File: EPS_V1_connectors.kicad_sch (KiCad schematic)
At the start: 29 parts, among them J1 Conn_01x20_Socket, J2 Conn_01x30_Socket, J3 Conn_01x15_Socket, J4 Conn_01x04_Socket, SW1 SWITCH, SW2 SWITCH, SW3 SWITCH, U4 MP28167GQ-Z

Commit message: Clean up & add labels
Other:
- note added: "CHARGING INPUT"
- note added: "CHARGING OUTPUT"
- note added: "CONNECTORS"
- note added: "GROUND LEG INHIBIT"
- note added: "SOLAR VOLTAGE REGULATOR"
- moved on the sheet: D1, D2, D3, D4, D5, D6, J1, J2, J3, J4, SW1, SW2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

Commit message: Add notes from Harvey meeting
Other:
- note added: "MOS enable"
- note added: "MOSFET bridge, look for low RDS on MOSFET: BUK7M15-60EX Chip: https://www.analog.com/en/products/lt4322.html"

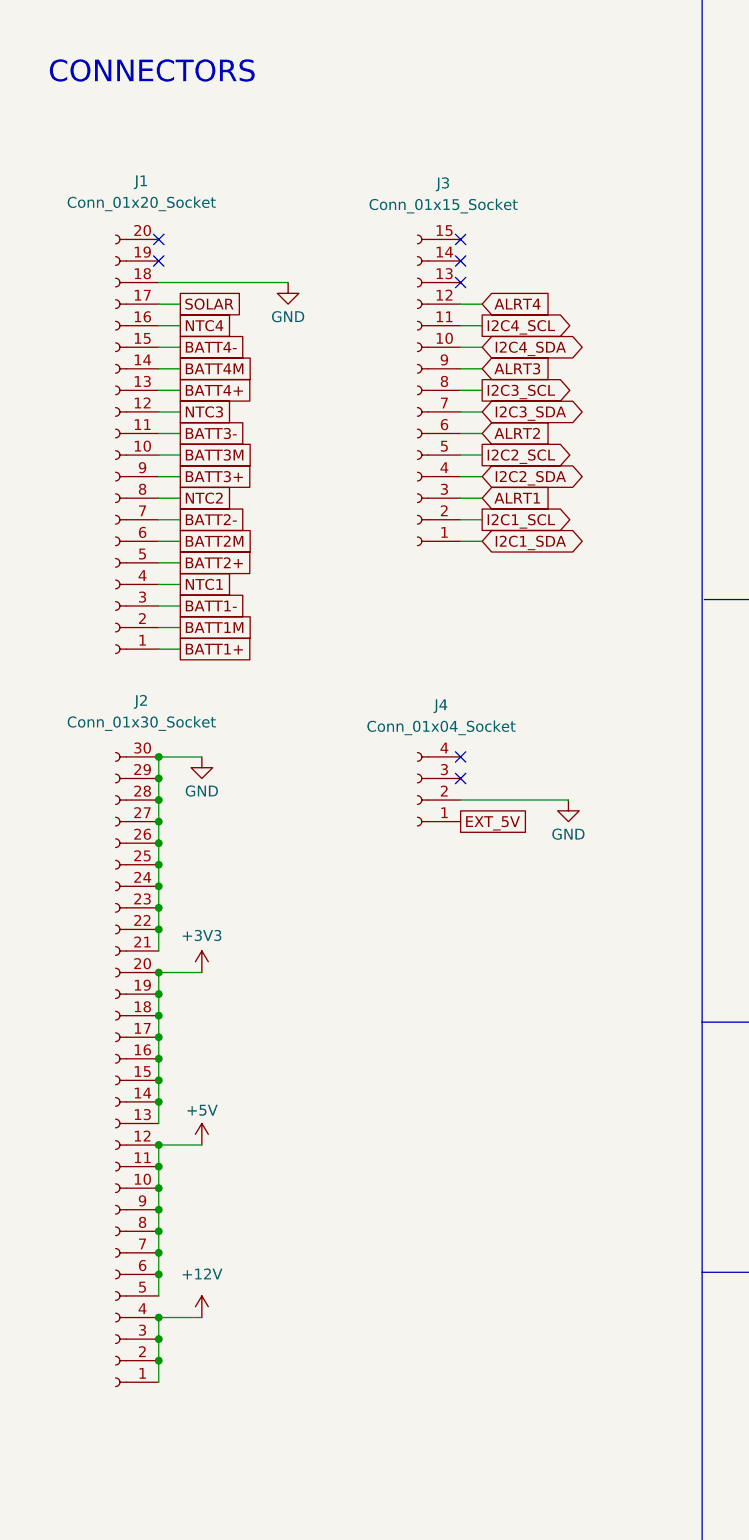
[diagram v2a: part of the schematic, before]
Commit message: assigned footprints to headers
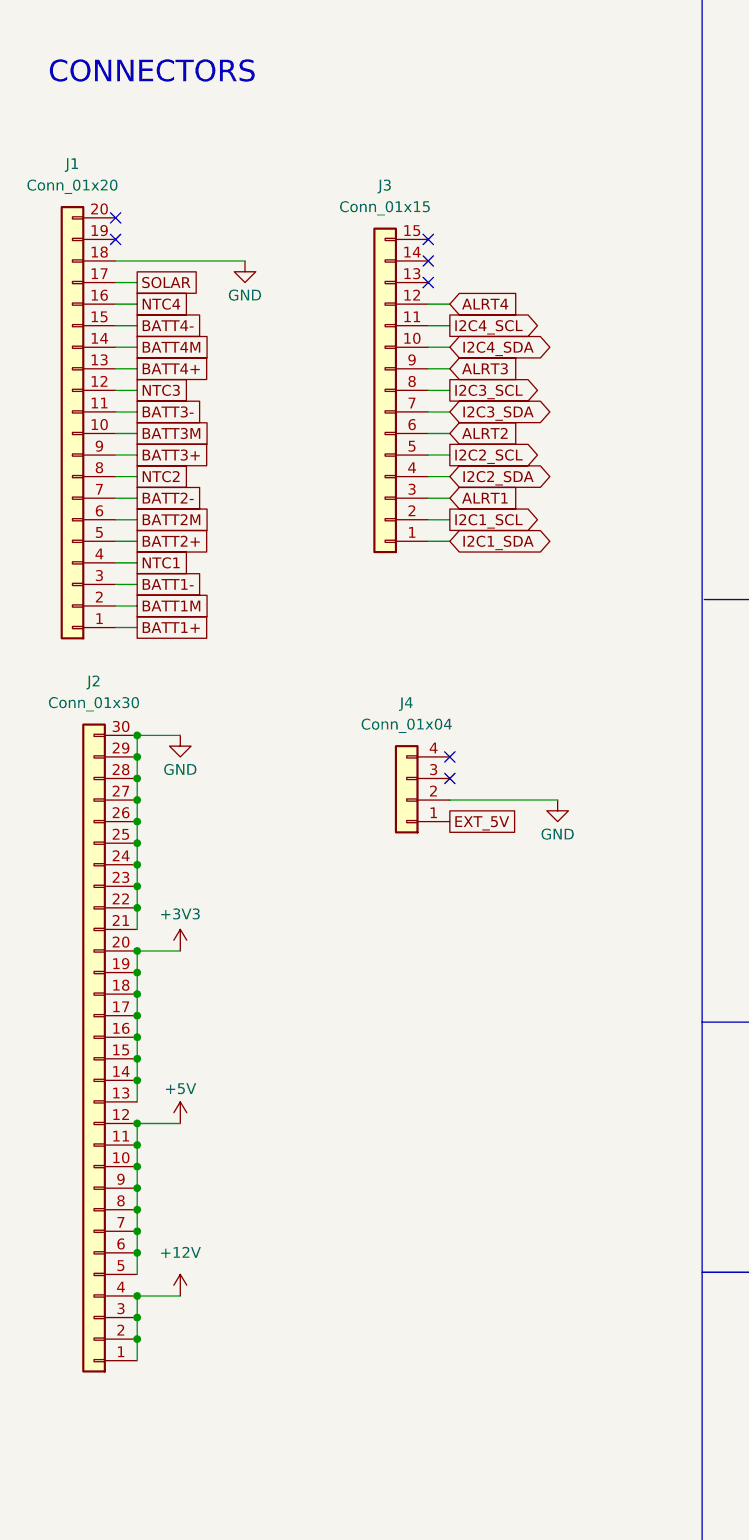
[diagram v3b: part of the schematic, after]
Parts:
- removed J1: Conn_01x20_Socket, symbol Connector:Conn_01x20_Socket
- removed J2: Conn_01x30_Socket, symbol Connector:Conn_01x30_Socket
- removed J3: Conn_01x15_Socket, symbol Connector:Conn_01x15_Socket
- removed J4: Conn_01x04_Socket, symbol Connector:Conn_01x04_Socket
- added J1: Conn_01x20, Connector_IDC:IDC-Header_2x10_P2.54mm_Latch6.5mm_Vertical, symbol Connector_Generic:Conn_01x20
- added J2: Conn_01x30, Connector_PinHeader_2.54mm:PinHeader_1x30_P2.54mm_Vertical, symbol Connector_Generic:Conn_01x30
- added J3: Conn_01x15, symbol Connector_Generic:Conn_01x15
- added J4: Conn_01x04, Connector_PinHeader_2.54mm:PinHeader_1x04_P2.54mm_Vertical, symbol Connector_Generic:Conn_01x04
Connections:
- net ALRT1: now also J3.3 (Pin_3)
- net ALRT2: now also J3.6 (Pin_6)
- net ALRT3: now also J3.9 (Pin_9)
- net ALRT4: now also J3.12 (Pin_12)
- net BATT1+: now also J1.1 (Pin_1)
- net BATT1-: now also J1.3 (Pin_3)
- net BATT1M: now also J1.2 (Pin_2)
- net BATT2+: now also J1.5 (Pin_5)
- net BATT2-: now also J1.7 (Pin_7)
- net BATT2M: now also J1.6 (Pin_6)
- net BATT3+: now also J1.9 (Pin_9)
- net BATT3-: now also J1.11 (Pin_11)
- net BATT3M: now also J1.10 (Pin_10)
- net BATT4+: now also J1.13 (Pin_13)
- net BATT4-: now also J1.15 (Pin_15)
- net BATT4M: now also J1.14 (Pin_14)
- net EXT_5V: now also J4.1 (Pin_1)
- net GND: now also J1.18 (Pin_18), J2.21 (Pin_21), J2.22 (Pin_22), J2.23 (Pin_23), J2.24 (Pin_24), J2.25 (Pin_25), J2.26 (Pin_26), J2.27 (Pin_27), J2.28 (Pin_28), J2.29 (Pin_29), J2.30 (Pin_30), J4.2 (Pin_2)
- net I2C1_SCL: now also J3.2 (Pin_2)
- net I2C1_SDA: now also J3.1 (Pin_1)
- net I2C2_SCL: now also J3.5 (Pin_5)
- net I2C2_SDA: now also J3.4 (Pin_4)
- net I2C3_SCL: now also J3.8 (Pin_8)
- net I2C3_SDA: now also J3.7 (Pin_7)
- net I2C4_SCL: now also J3.11 (Pin_11)
- net I2C4_SDA: now also J3.10 (Pin_10)
- net NTC1: now also J1.4 (Pin_4)
- net NTC2: now also J1.8 (Pin_8)
- net NTC3: now also J1.12 (Pin_12)
- net NTC4: now also J1.16 (Pin_16)
- net SOLAR: now also J1.17 (Pin_17)
- new net: J2.1 (Pin_1), J2.2 (Pin_2), J2.3 (Pin_3), J2.4 (Pin_4)
- new net: J2.10 (Pin_10), J2.11 (Pin_11), J2.12 (Pin_12), J2.5 (Pin_5), J2.6 (Pin_6), J2.7 (Pin_7), J2.8 (Pin_8), J2.9 (Pin_9)
- new net: J2.13 (Pin_13), J2.14 (Pin_14), J2.15 (Pin_15), J2.16 (Pin_16), J2.17 (Pin_17), J2.18 (Pin_18), J2.19 (Pin_19), J2.20 (Pin_20)

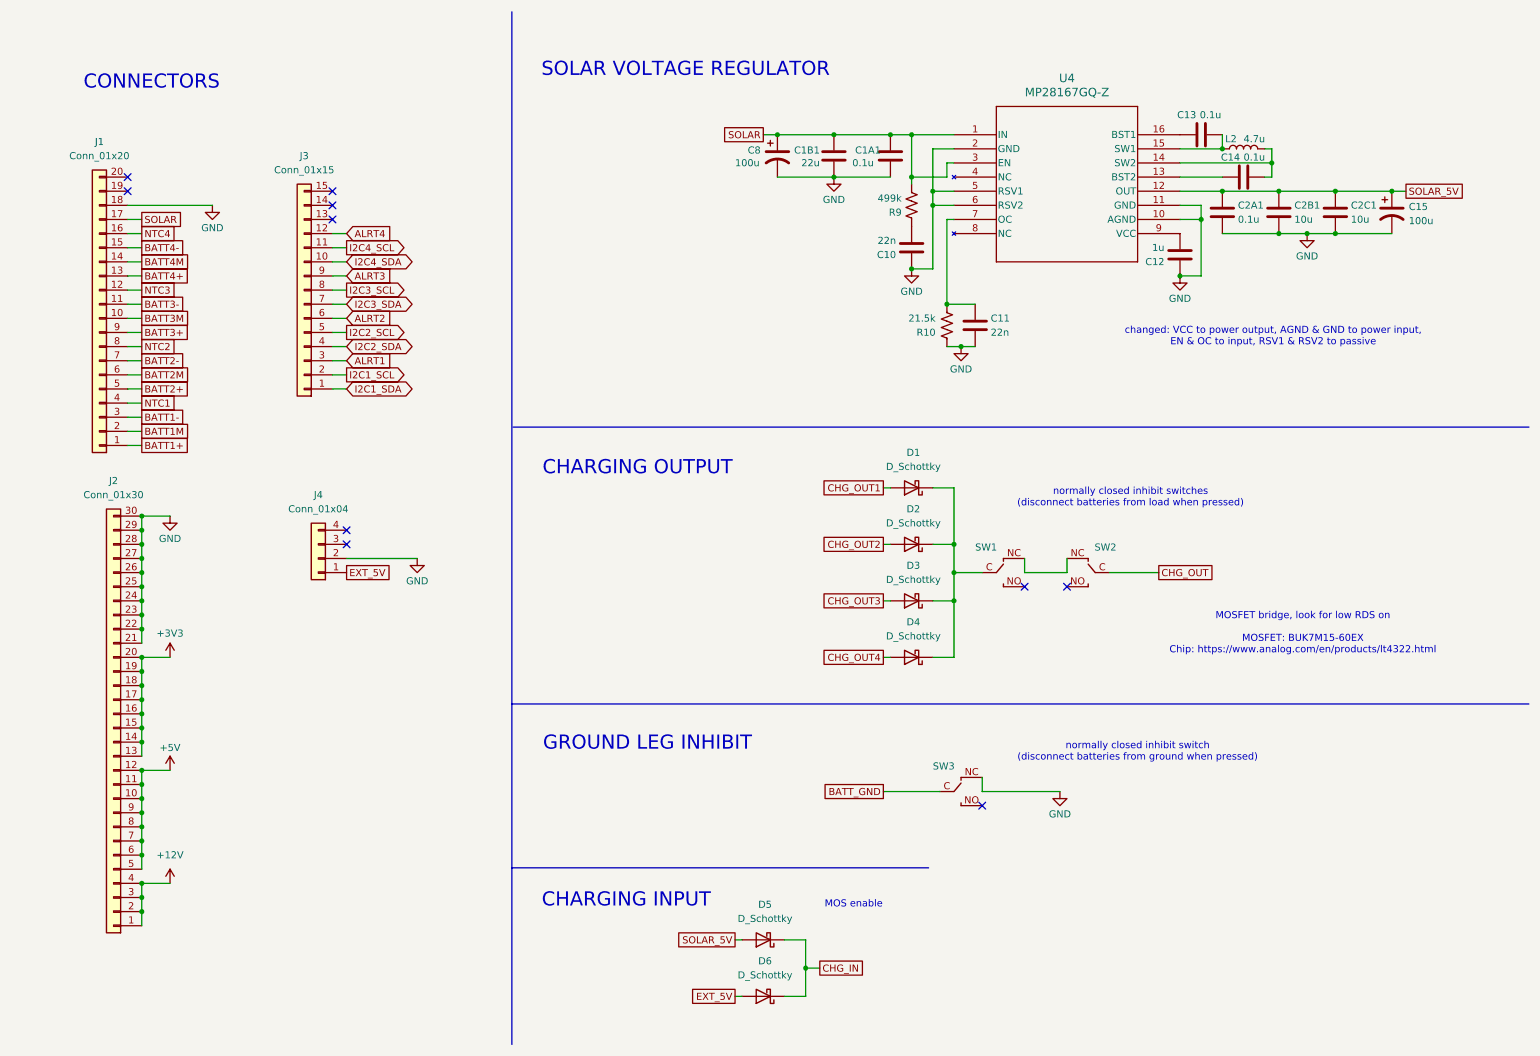
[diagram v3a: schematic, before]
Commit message: Add power switching IC
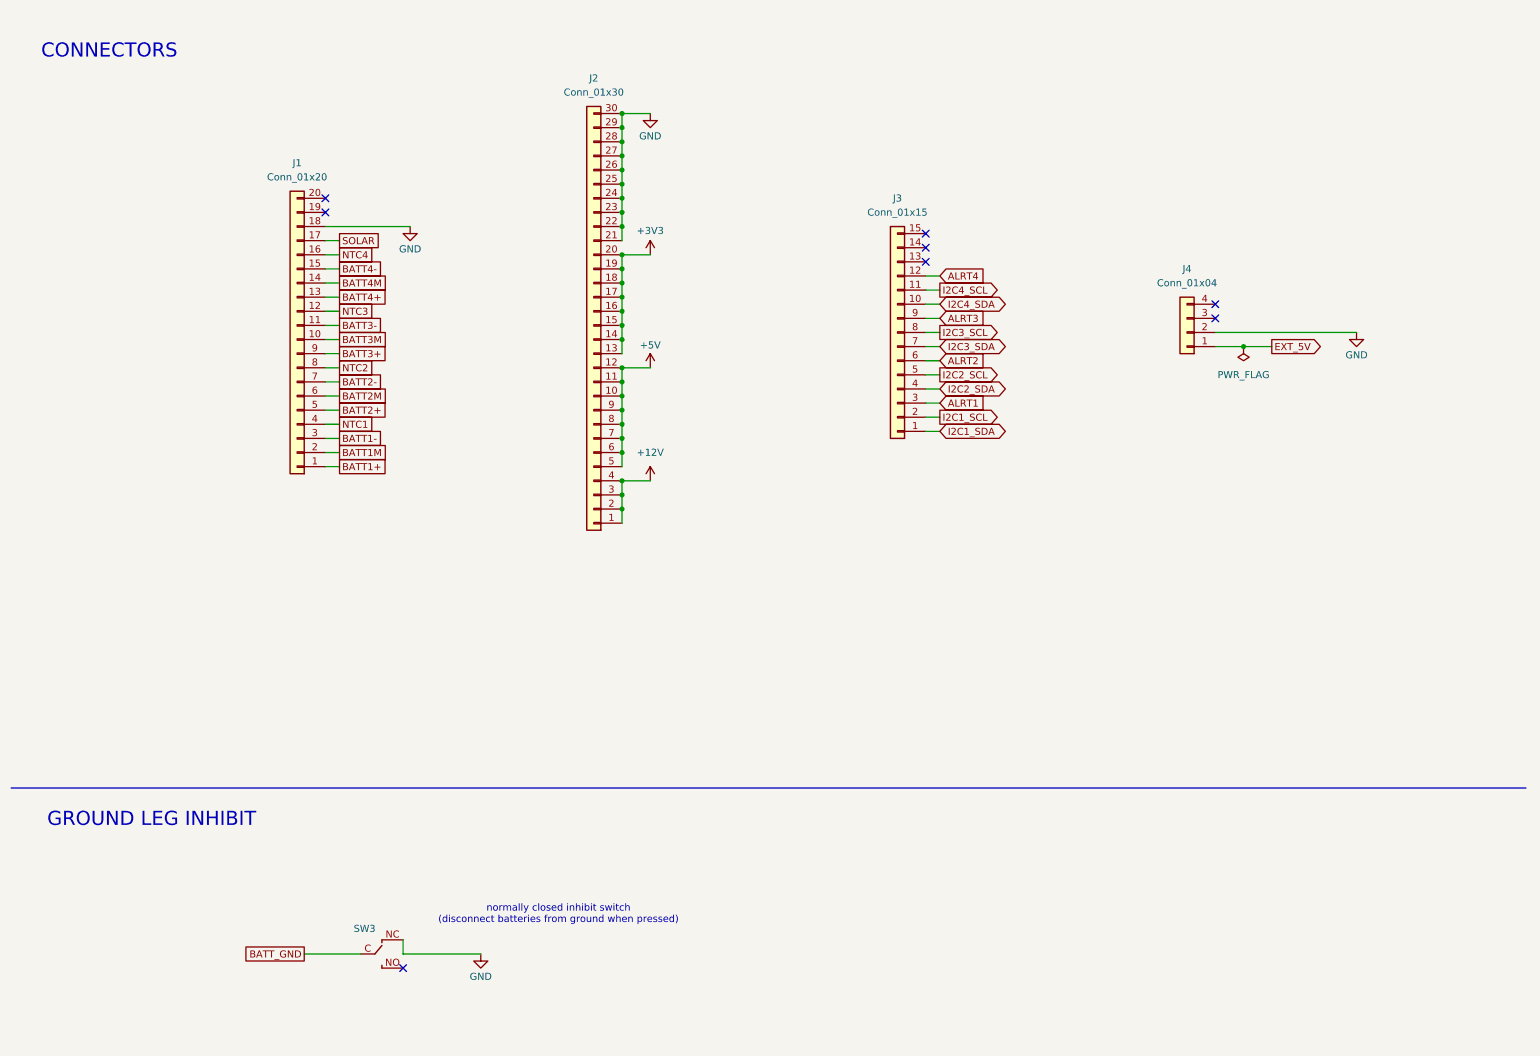
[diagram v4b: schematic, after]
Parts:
- removed C10, C11: 22n, Capacitor_SMD:C_0603_1608Metric, symbol Device:C
- removed C12: 1u, Capacitor_SMD:C_0603_1608Metric, symbol Device:C
- removed C13, C14, C1A1, C2A1: 0.1u, Capacitor_SMD:C_0603_1608Metric, symbol Device:C
- removed C15, C8: 100u, Capacitor_SMD:CP_Elec_6.3x5.4, symbol Device:C_Polarized_US
- removed C1B1: 22u, Capacitor_SMD:C_0805_2012Metric, symbol Device:C
- removed C2B1, C2C1: 10u, Capacitor_SMD:C_0805_2012Metric, symbol Device:C
- removed D1, D2, D3, D4, D5, D6: D_Schottky, Diode_SMD:D_SOD-128, symbol Device:D_Schottky
- removed L2: 4.7u, ASPI_7318_4R7M_T:IND_ASPI-7318-4R7M-T, symbol Device:L
- removed R10: 21.5k, Resistor_SMD:R_0603_1608Metric, symbol Device:R_US
- removed R9: 499k, Resistor_SMD:R_0603_1608Metric, symbol Device:R_US
- removed SW1: SWITCH, oresat-misc:D2F-L3-D-HORIZONTAL-R, symbol oresat-misc:OMRON-D2F-L3-D-RIGHT
- removed SW2: SWITCH, oresat-misc:D2F-L3-D-HORIZONTAL-L, symbol oresat-misc:OMRON-D2F-L3-D-LEFT
- removed U4: MP28167GQ-Z, MP28167GQ-Z:QFN-16_MP28167GQ_MNP, symbol MP28167GQ-Z:MP28167GQ-Z
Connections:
- no-connect marks 10 -> 8
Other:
- note removed: "CHARGING INPUT"
- note removed: "CHARGING OUTPUT"
- note removed: "MOS enable"
- note removed: "MOSFET bridge, look for low RDS on MOSFET: BUK7M15-60EX Chip: https://www.analog.com/en/products/lt4322.html"
- note removed: "SOLAR VOLTAGE REGULATOR"
- note removed: "changed: VCC to power output, AGND & GND to power input, EN & OC to input, RSV1 & RSV2 to passive"
- note removed: "normally closed inhibit switches (disconnect batteries from load when pressed)"
- moved on the sheet: J1, J2, J3, J4, SW3

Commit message: Add other battery packs, connect all ALRT signals, assign footprints for new components, make inhibit switch footprints
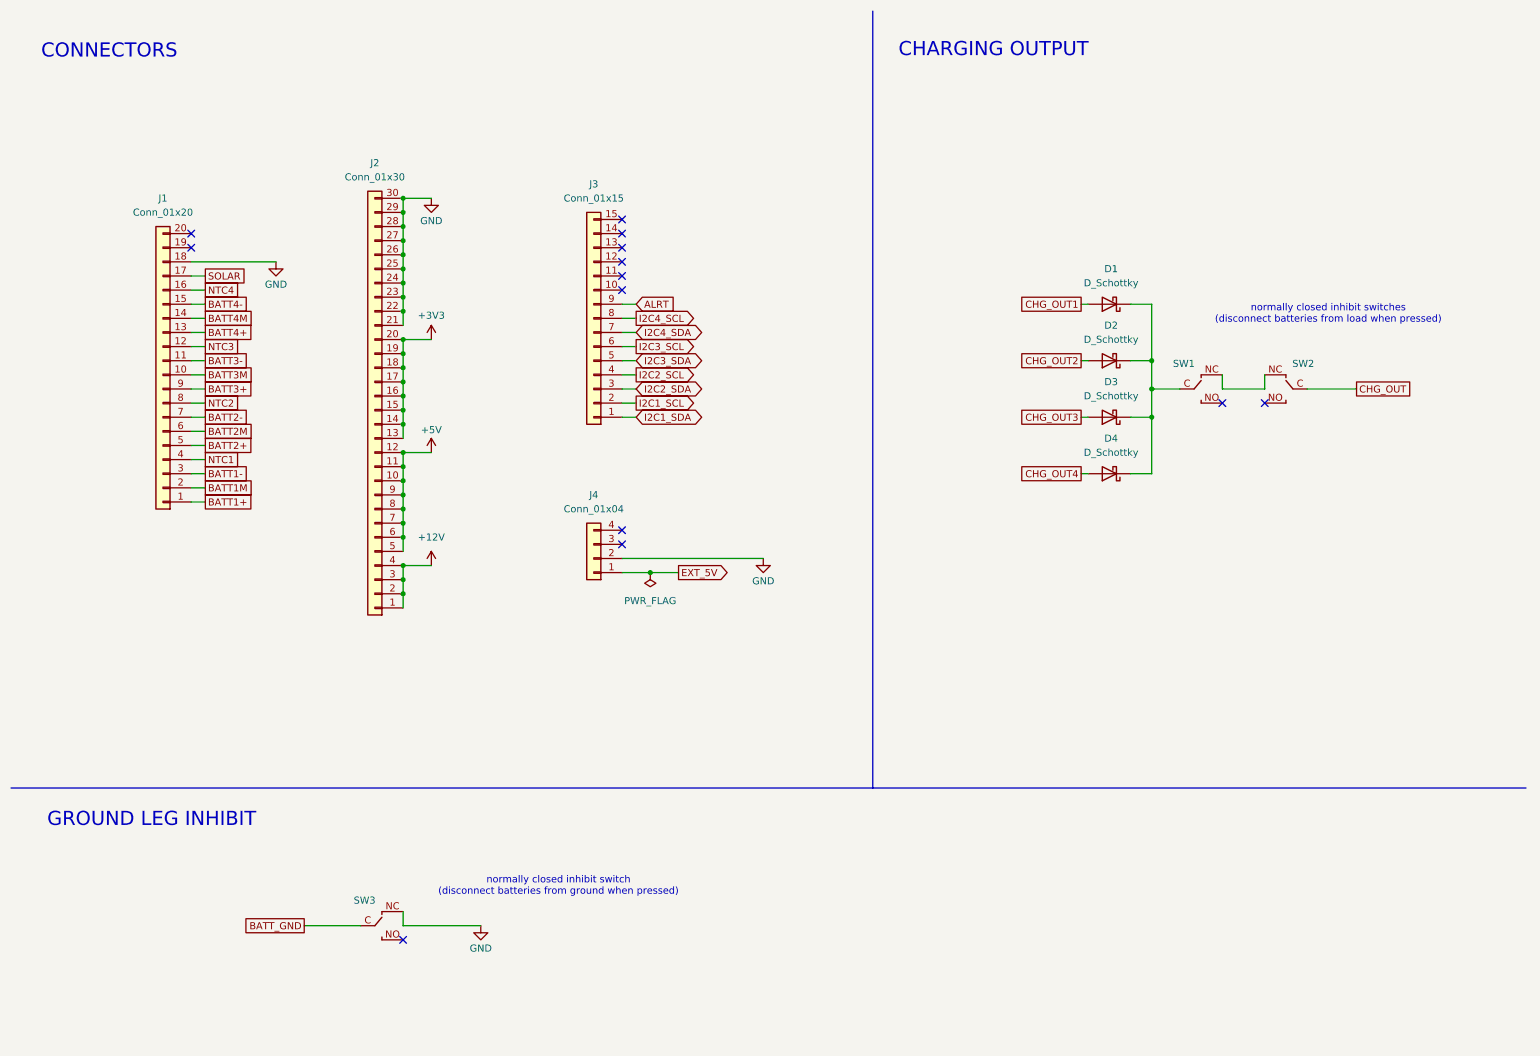
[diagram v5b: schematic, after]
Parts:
- added D1, D2, D3, D4: D_Schottky, Diode_SMD:D_SOD-128, symbol Device:D_Schottky
- added SW1: SWITCH, switches:D2F-L3-D-HORIZONTAL-R, symbol oresat-misc:OMRON-D2F-L3-D-RIGHT
- added SW2: SWITCH, switches:D2F-L3-D-HORIZONTAL-L, symbol oresat-misc:OMRON-D2F-L3-D-LEFT
- J3: footprint (none) -> Connector_PinHeader_2.54mm:PinHeader_1x15_P2.54mm_Vertical
- SW3: footprint oresat-misc:D2F-L3-D-HORIZONTAL-R -> switches:D2F-L3-D-HORIZONTAL-R
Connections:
- net ALRT1 is gone; now on net I2C2_SDA: J3.3 (Pin_3)
- net ALRT2 is gone; now on net I2C3_SCL: J3.6 (Pin_6)
- net I2C2_SCL: now also J3.4 (Pin_4); no longer J3.5 (Pin_5)
- net I2C2_SDA: no longer J3.4 (Pin_4)
- net I2C3_SCL: no longer J3.8 (Pin_8)
- net I2C3_SDA: now also J3.5 (Pin_5); no longer J3.7 (Pin_7)
- net I2C4_SCL: now also J3.8 (Pin_8); no longer J3.11 (Pin_11)
- net I2C4_SDA: now also J3.7 (Pin_7); no longer J3.10 (Pin_10)
- net ALRT3 renamed ALRT
- net ALRT4: no longer names the net of J3.12 (Pin_12)
- new net: D1.1 (K), D2.1 (K), D3.1 (K), D4.1 (K), SW1.C (COM)
- new net: SW1.NC, SW2.NC
- new net CHG_OUT: SW2.C (COM)
- new net CHG_OUT1: D1.2 (A)
- new net CHG_OUT2: D2.2 (A)
- new net CHG_OUT3: D3.2 (A)
- new net CHG_OUT4: D4.2 (A)
- no-connect marks 8 -> 13
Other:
- note added: "CHARGING OUTPUT"
- note added: "normally closed inhibit switches (disconnect batteries from load when pressed)"
- moved on the sheet: J1, J2, J3, J4, SW3
